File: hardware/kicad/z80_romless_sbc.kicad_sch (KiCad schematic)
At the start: 41 parts, among them J1 REGULATED 5V INPUT, J2 PICO GPIO EXPANSION, U1 Z84C0020PEC, U10 SN74LVC245AN bus-to-Pico, U2 AS6C1008-55PCN, U3 SN74HCT32N, U4 SN74AHCT244N, U7 SN74LVC244AN, U9 SN74AHCT245N Pico-to-bus

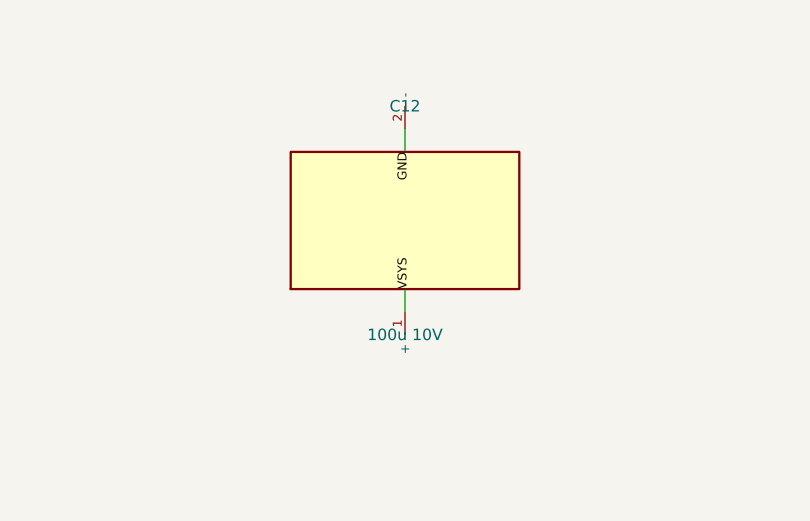
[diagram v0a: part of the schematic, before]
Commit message: Fix USB-disconnect resets and remove trial VSYS capacitor
Check the settled IORQ# level before validating RD#/WR# in the I/O
trap. Ignore inactive interrupt events and resume the Z80 clock
instead of treating them as malformed requests and rebooting.

- Count inactive interrupts while preserving control-error
  qualification checks.
- Retain fail-closed handling for invalid active requests and
  I/O release timeouts.
- Preserve the trap fault reason and GPIO snapshot across watchdog
  resets and expose them through Stage 9 diagnostics.
- Recheck USB connectivity before each transmitted console byte.
- Add regressions for inactive interrupts, subsequent valid I/O,
  retained reset faults, and disconnects during sustained output.

Remove the trial C12 VSYS capacitor from the schematic generator,
schematic, BOM, netlists, exports, and breadboard diagram. Update
inventory and wiring instructions to restore 11 external capacitors
and one 100 uF supply-entry capacitor. Leave the deferred PCB and
fabrication files unchanged.

Keep documentation focused on the current design and behaviour,
without the capacitor experiment or resolved-incident narrative.

Validation:
- All 11 focused control and Stage 9 host tests passed.
- Affected Stage 8, Stage 9, and Stage 10 firmware targets built.
- Schematic ERC passed with zero violations.
- Netlist parity passed: 71 nets and 284 component pin endpoints.
- Strict MkDocs build and whitespace checks passed.

Co-authored-by: Copilot <223556219+Copilot@users.noreply.github.com>
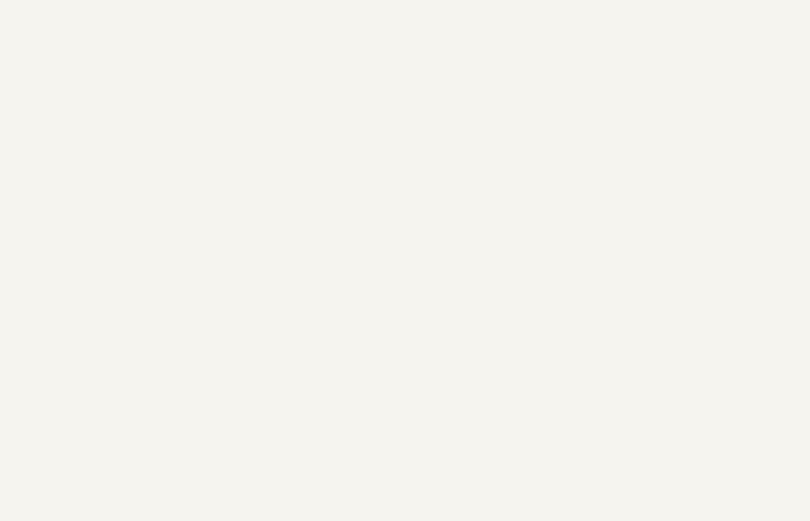
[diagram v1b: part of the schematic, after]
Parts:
- removed C12: 100u 10V, Capacitor_THT:CP_Radial_D10.0mm_P5.00mm, symbol Z80SBC:CAPACITOR

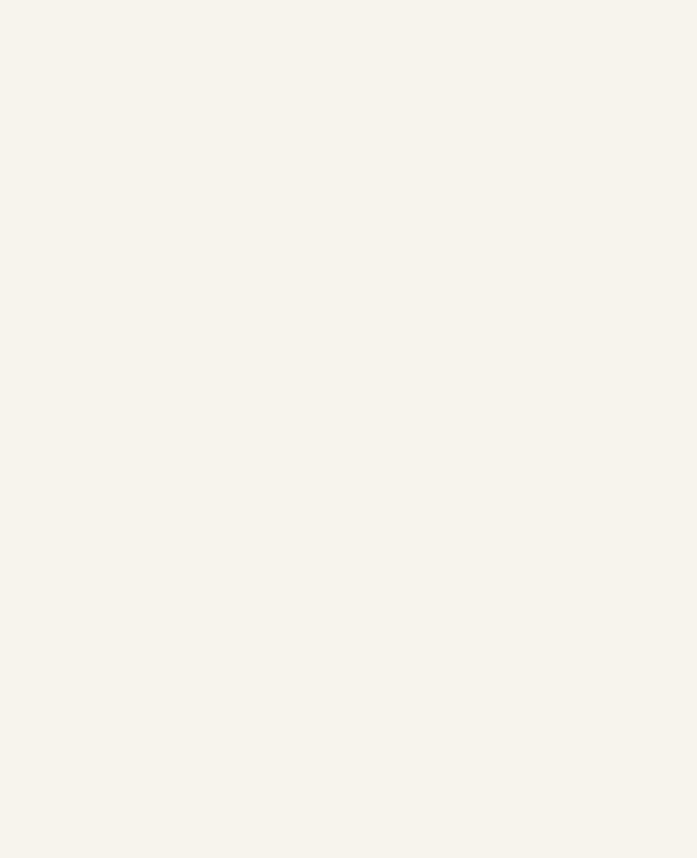
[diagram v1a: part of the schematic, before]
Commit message: docs(hardware): reflect Stage 10 matrix display in docs and schematic
- Correct the Stage 10 wiring summary and update inventory and pin mapping
- Add the external HT16K33 8x8 matrix as A2 with GP22 SDA, GP26 SCL,
  3.3 V power and common ground
- Document backpack pin markings, pull-up safety and bench-tested operation
- Extend net assertions and regenerate schematic exports, BOM and netlists
- Leave deferred PCB, routing and fabrication files unchanged

Validated with zero ERC violations, exact netlist parity,
documentation interconnect checks and a strict MkDocs build.

Co-authored-by: Copilot <223556219+Copilot@users.noreply.github.com>
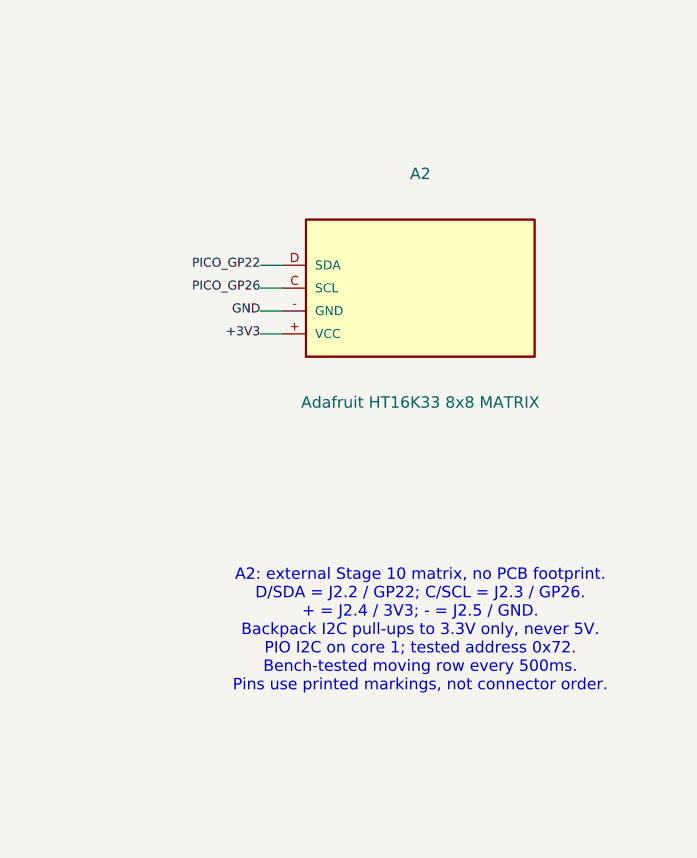
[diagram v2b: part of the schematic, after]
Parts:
- added A2: Adafruit HT16K33 8x8 MATRIX, symbol Z80SBC:HT16K33_MATRIX
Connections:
- net +3V3: now also A2.+ (VCC)
- net GND: now also A2.- (GND)
- net PICO_GP22: now also A2.D (SDA)
- net PICO_GP26: now also A2.C (SCL)
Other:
- note added: "A2: external Stage 10 matrix, no PCB footprint. D/SDA = J2.2 / GP22; C/SCL = J2.3 / GP26. + = J2.4 / 3V3; - = J2.5 / GND. Backpack I2C pull-ups to 3.3V only, never 5V. PIO I2C on core 1; tested address 0x72. Bench-tested moving row every 500ms. Pins use printed markings, not connector order."
